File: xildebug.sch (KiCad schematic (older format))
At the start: 36 parts, among them J1 USB_B_Micro, J2 Conn_STM_SWD, J3 Conn_Ext1, J4 Conn_Ext2, J5 Conn_DUT, J6 Conn_DUT_VDD, U1 XC6206P332MR, U2 MAX14662, U3 STM32L433CCUx

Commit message: Changed the USB data pin names to match the USB connector convention
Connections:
- net USB_DM renamed USB_D+
- net USB_D+: now also J1.3 (D+); no longer J1.2 (D-)
- net USB_DP renamed USB_D-
- net USB_D-: now also J1.2 (D-); no longer J1.3 (D+)
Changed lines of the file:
@@
 Text Label 6400 5250 0    50   ~ 0
 GPIO3_A
+Text Label 4650 4250 2    50   ~ 0
+USB_D+
 Text Label 4650 4350 2    50   ~ 0
-USB_DP
-Text Label 4650 4250 2    50   ~ 0
-USB_DM
+USB_D-
 Text Label 5200 3750 2    50   ~ 0
 STM_SWDIO
@@
 $EndComp
 Text Label 2150 1650 0    50   ~ 0
-USB_DP
+USB_D+
 Text Label 2150 1750 0    50   ~ 0
-USB_DM
+USB_D-
 NoConn ~ 2100 1850
 Wire Wire Line

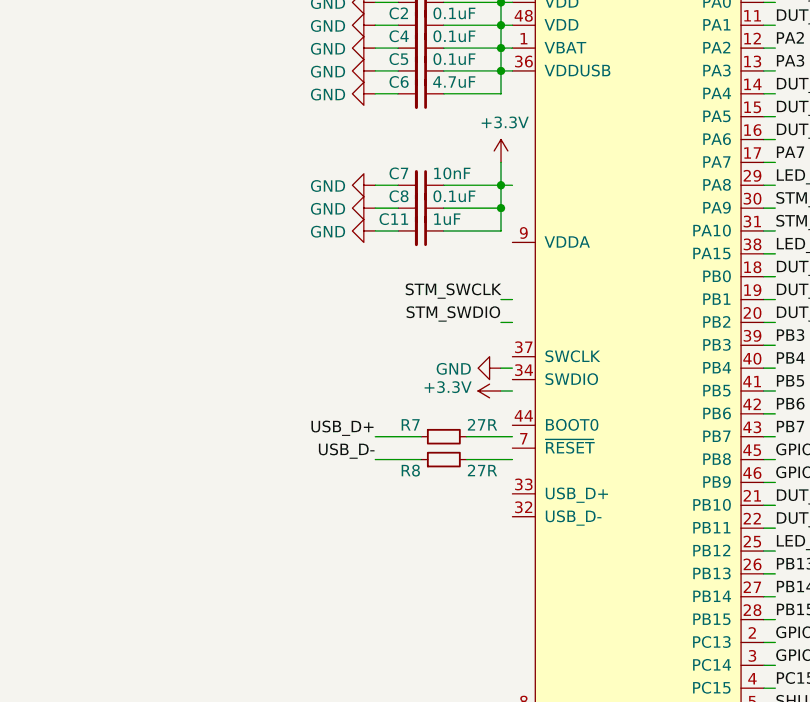
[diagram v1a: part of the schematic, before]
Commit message: Add ferrite bead on the VDDA of the STM
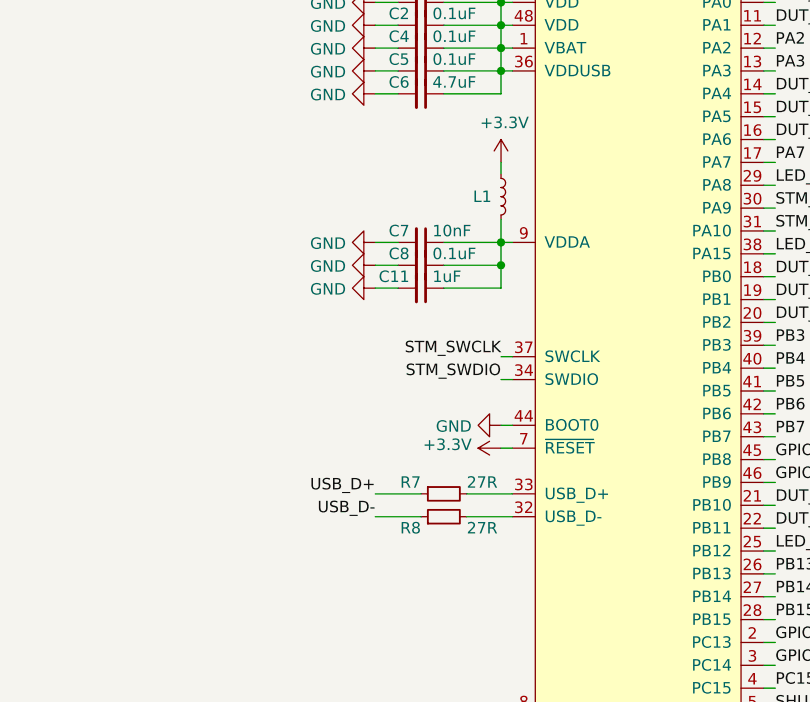
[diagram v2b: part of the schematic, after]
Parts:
- added L1: FB, symbol Device:L_Small
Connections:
- net +3V3: now also U3.7 (~RESET~), L1.2; no longer C11.1, C7.1, C8.1
- net GND: now also U3.44 (BOOT0)
- net STM_SWCLK: now also U3.37 (SWCLK)
- net STM_SWDIO: now also U3.34 (SWDIO)
- net at U3.32 (USB_D-): now also R8.2
- net at U3.33 (USB_D+): now also R7.2
- net at U3.9 (VDDA): now also C11.1, C7.1, C8.1, L1.1
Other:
- moved on the sheet: C11, C7, C8, R7, R8
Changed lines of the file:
@@
 $EndComp
 Wire Wire Line
-	5250 3750 5200 3750
-Wire Wire Line
-	5250 3650 5200 3650
+	5250 4000 5200 4000
+Wire Wire Line
+	5250 3900 5200 3900
 $Comp
 L Connector_Generic:Conn_01x06 J5
@@
 Text Label 6400 5250 0    50   ~ 0
 GPIO3_A
-Text Label 4650 4250 2    50   ~ 0
+Text Label 4650 4500 2    50   ~ 0
 USB_D+
-Text Label 4650 4350 2    50   ~ 0
+Text Label 4650 4600 2    50   ~ 0
 USB_D-
-Text Label 5200 3750 2    50   ~ 0
+Text Label 5200 4000 2    50   ~ 0
 STM_SWDIO
-Text Label 5200 3650 2    50   ~ 0
+Text Label 5200 3900 2    50   ~ 0
 STM_SWCLK
 $Comp
@@
 L Device:R_Small R8
 U 1 1 5B52EFB9
-P 4950 4350
-F 0 "R8" V 4900 4450 50  0000 L CNN
-F 1 "27R" V 4900 4250 50  0000 R CNN
-F 2 "Resistor_SMD:R_0603_1608Metric" H 4950 4350 50  0001 C CNN
-F 3 "~" H 4950 4350 50  0001 C CNN
-	1    4950 4350
+P 4950 4600
+F 0 "R8" V 4900 4700 50  0000 L CNN
+F 1 "27R" V 4900 4500 50  0000 R CNN
+F 2 "Resistor_SMD:R_0603_1608Metric" H 4950 4600 50  0001 C CNN
+F 3 "~" H 4950 4600 50  0001 C CNN
+	1    4950 4600
 	0    -1   -1   0
 $EndComp
@@
 L Device:R_Small R7
 U 1 1 5B52F1AA
-P 4950 4250
-F 0 "R7" V 4900 4350 50  0000 L CNN
-F 1 "27R" V 4900 4150 50  0000 R CNN
-F 2 "Resistor_SMD:R_0603_1608Metric" H 4950 4250 50  0001 C CNN
-F 3 "~" H 4950 4250 50  0001 C CNN
-	1    4950 4250
+P 4950 4500
+F 0 "R7" V 4900 4600 50  0000 L CNN
+F 1 "27R" V 4900 4400 50  0000 R CNN
+F 2 "Resistor_SMD:R_0603_1608Metric" H 4950 4500 50  0001 C CNN
+F 3 "~" H 4950 4500 50  0001 C CNN
+	1    4950 4500
 	0    -1   1    0
 $EndComp
 Wire Wire Line
-	5050 4350 5250 4350
-Wire Wire Line
-	5050 4250 5250 4250
-Wire Wire Line
-	4650 4350 4850 4350
-Wire Wire Line
-	4650 4250 4850 4250
+	5050 4600 5250 4600
+Wire Wire Line
+	5050 4500 5250 4500
+Wire Wire Line
+	4650 4600 4850 4600
+Wire Wire Line
+	4650 4500 4850 4500
 Wire Wire Line
 	9950 2900 10000 2900
@@
 Connection ~ 5200 5550
 Wire Wire Line
-	5250 3950 5200 3950
-Wire Wire Line
-	5250 4050 5200 4050
+	5250 4200 5200 4200
+Wire Wire Line
+	5250 4300 5200 4300
 Wire Wire Line
 	5250 2350 5200 2350
@@
 Connection ~ 5200 2550
 Wire Wire Line
-	5250 3150 5200 3150
-Wire Wire Line
-	5200 3150 5200 3050
+	5250 3400 5200 3400
 Connection ~ 5200 2650
 Wire Wire Line
 	5200 2750 5200 2650
-Connection ~ 5200 3150
-Wire Wire Line
-	5200 3150 5200 3250
-Wire Wire Line
-	5200 3250 5200 3350
-Connection ~ 5200 3250
+Connection ~ 5200 3400
+Wire Wire Line
+	5200 3400 5200 3500
+Wire Wire Line
+	5200 3500 5200 3600
+Connection ~ 5200 3500
 $Comp
 L power:+3.3V #PWR06
@@
 	4950 2450 5200 2450
 Wire Wire Line
-	4950 3150 5200 3150
-Wire Wire Line
-	4950 3250 5200 3250
-Wire Wire Line
-	4950 3350 5200 3350
+	4950 3400 5200 3400
+Wire Wire Line
+	4950 3500 5200 3500
+Wire Wire Line
+	4950 3600 5200 3600
 $Comp
 L power:GND #PWR08
@@
 L Device:C_Small C8
 U 1 1 5AF46D36
-P 4850 3250
-F 0 "C8" V 4800 3200 50  0000 R CNN
-F 1 "0.1uF" V 4800 3300 50  0000 L CNN
-F 2 "Capacitor_SMD:C_0603_1608Metric" H 4850 3250 50  0001 C CNN
-F 3 "~" H 4850 3250 50  0001 C CNN
-	1    4850 3250
+P 4850 3500
+F 0 "C8" V 4800 3450 50  0000 R CNN
+F 1 "0.1uF" V 4800 3550 50  0000 L CNN
+F 2 "Capacitor_SMD:C_0603_1608Metric" H 4850 3500 50  0001 C CNN
+F 3 "~" H 4850 3500 50  0001 C CNN
+	1    4850 3500
 	0    1    1    0
 $EndComp
@@
 L Device:C_Small C7
 U 1 1 5AF46DB8
-P 4850 3150
-F 0 "C7" V 4800 3100 50  0000 R CNN
-F 1 "10nF" V 4800 3200 50  0000 L CNN
-F 2 "Capacitor_SMD:C_0603_1608Metric" H 4850 3150 50  0001 C CNN
-F 3 "~" H 4850 3150 50  0001 C CNN
-	1    4850 3150
+P 4850 3400
+F 0 "C7" V 4800 3350 50  0000 R CNN
+F 1 "10nF" V 4800 3450 50  0000 L CNN
+F 2 "Capacitor_SMD:C_0603_1608Metric" H 4850 3400 50  0001 C CNN
+F 3 "~" H 4850 3400 50  0001 C CNN
+	1    4850 3400
 	0    1    1    0
 $EndComp
@@
 L Device:C_Small C11
 U 1 1 5AF46E6F
-P 4850 3350
-F 0 "C11" V 4800 3300 50  0000 R CNN
-F 1 "1uF" V 4800 3400 50  0000 L CNN
-F 2 "Capacitor_SMD:C_0603_1608Metric" H 4850 3350 50  0001 C CNN
-F 3 "~" H 4850 3350 50  0001 C CNN
-	1    4850 3350
-	0    1    1    0
-$EndComp
-Wire Wire Line
-	4750 3150 4650 3150
-Wire Wire Line
-	4750 3250 4650 3250
-Wire Wire Line
-	4750 3350 4650 3350
+P 4850 3600
+F 0 "C11" V 4800 3550 50  0000 R CNN
+F 1 "1uF" V 4800 3650 50  0000 L CNN
+F 2 "Capacitor_SMD:C_0603_1608Metric" H 4850 3600 50  0001 C CNN
+F 3 "~" H 4850 3600 50  0001 C CNN
+	1    4850 3600
+	0    1    1    0
+$EndComp
+Wire Wire Line
+	4750 3400 4650 3400
+Wire Wire Line
+	4750 3500 4650 3500
+Wire Wire Line
+	4750 3600 4650 3600
 $Comp
 L power:GND #PWR020
 U 1 1 5AF5E9A3
-P 4650 3150
-F 0 "#PWR020" H 4650 2900 50  0001 C CNN
-F 1 "GND" V 4655 3022 50  0000 R CNN
-F 2 "" H 4650 3150 50  0001 C CNN
-F 3 "" H 4650 3150 50  0001 C CNN
-	1    4650 3150
+P 4650 3400
+F 0 "#PWR020" H 4650 3150 50  0001 C CNN
+F 1 "GND" V 4655 3272 50  0000 R CNN
+F 2 "" H 4650 3400 50  0001 C CNN
+F 3 "" H 4650 3400 50  0001 C CNN
+	1    4650 3400
 	0    1    1    0
 $EndComp
@@
 L power:GND #PWR021
 U 1 1 5AF5EA1C
-P 4650 3250
-F 0 "#PWR021" H 4650 3000 50  0001 C CNN
-F 1 "GND" V 4655 3122 50  0000 R CNN
-F 2 "" H 4650 3250 50  0001 C CNN
-F 3 "" H 4650 3250 50  0001 C CNN
-	1    4650 3250
+P 4650 3500
+F 0 "#PWR021" H 4650 3250 50  0001 C CNN
+F 1 "GND" V 4655 3372 50  0000 R CNN
+F 2 "" H 4650 3500 50  0001 C CNN
+F 3 "" H 4650 3500 50  0001 C CNN
+	1    4650 3500
 	0    1    1    0
 $EndComp
@@
 L power:GND #PWR023
 U 1 1 5AF5EA9A
-P 4650 3350
-F 0 "#PWR023" H 4650 3100 50  0001 C CNN
-F 1 "GND" V 4655 3222 50  0000 R CNN
-F 2 "" H 4650 3350 50  0001 C CNN
-F 3 "" H 4650 3350 50  0001 C CNN
-	1    4650 3350
+P 4650 3600
+F 0 "#PWR023" H 4650 3350 50  0001 C CNN
+F 1 "GND" V 4655 3472 50  0000 R CNN
+F 2 "" H 4650 3600 50  0001 C CNN
+F 3 "" H 4650 3600 50  0001 C CNN
+	1    4650 3600
 	0    1    1    0
 $EndComp
@@
 L power:+3.3V #PWR028
 U 1 1 5AFC13F1
-P 5200 4050
-F 0 "#PWR028" H 5200 3900 50  0001 C CNN
-F 1 "+3.3V" V 5215 4178 50  0000 L CNN
-F 2 "" H 5200 4050 50  0001 C CNN
-F 3 "" H 5200 4050 50  0001 C CNN
-	1    5200 4050
+P 5200 4300
+F 0 "#PWR028" H 5200 4150 50  0001 C CNN
+F 1 "+3.3V" V 5215 4428 50  0000 L CNN
+F 2 "" H 5200 4300 50  0001 C CNN
+F 3 "" H 5200 4300 50  0001 C CNN
+	1    5200 4300
 	0    -1   -1   0
 $EndComp
@@
 L power:GND #PWR0101
 U 1 1 5BB12C8D
-P 5200 3950
-F 0 "#PWR0101" H 5200 3700 50  0001 C CNN
-F 1 "GND" V 5205 3822 50  0000 R CNN
-F 2 "" H 5200 3950 50  0001 C CNN
-F 3 "" H 5200 3950 50  0001 C CNN
-	1    5200 3950
+P 5200 4200
+F 0 "#PWR0101" H 5200 3950 50  0001 C CNN
+F 1 "GND" V 5205 4072 50  0000 R CNN
+F 2 "" H 5200 4200 50  0001 C CNN
+F 3 "" H 5200 4200 50  0001 C CNN
+	1    5200 4200
 	0    1    1    0
 $EndComp
 Text Notes 9550 3800 2    50   ~ 0
 I2C: 0x98
+$Comp
+L Device:L_Small L1
+U 1 1 5BBB5951
+P 5200 3200
+F 0 "L1" H 5159 3200 50  0000 R CNN
+F 1 "FB" H 5159 3245 50  0001 R CNN
+F 2 "" H 5200 3200 50  0001 C CNN
+F 3 "~" H 5200 3200 50  0001 C CNN
+	1    5200 3200
+	1    0    0    1
+$EndComp
+Wire Wire Line
+	5200 3100 5200 3050
+Wire Wire Line
+	5200 3300 5200 3400
 $EndSCHEMATC

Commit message: Add footprint for the STM that works for QFN and QFP
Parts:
- L1: footprint (none) -> Inductor_SMD:L_0603_1608Metric
- U3: footprint Package_DFN_QFN:QFN-48-1EP_7x7mm_P0.5mm_EP5.15x5.15mm -> Package_DFN_QFN_Extra:UFQFPN-48-1EP_7x7mm_P0.5mm_EP5.15x5.15mm
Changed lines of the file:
@@
 F 0 "U3" H 6250 5700 50  0000 R CNN
 F 1 "STM32L433CCUx" H 5800 2200 50  0000 C CNN
-F 2 "Package_DFN_QFN:QFN-48-1EP_7x7mm_P0.5mm_EP5.15x5.15mm" H 5800 2100 50  0001 C CNN
+F 2 "Package_DFN_QFN_Extra:UFQFPN-48-1EP_7x7mm_P0.5mm_EP5.15x5.15mm" H 5800 2100 50  0001 C CNN
 F 3 "https://www.mouser.se/datasheet/2/389/stm32l433cc-956250.pdf" H 5800 2100 50  0001 C CNN
 	1    5800 3950
@@
 F 0 "L1" H 5159 3200 50  0000 R CNN
 F 1 "FB" H 5159 3245 50  0001 R CNN
-F 2 "" H 5200 3200 50  0001 C CNN
+F 2 "Inductor_SMD:L_0603_1608Metric" H 5200 3200 50  0001 C CNN
 F 3 "~" H 5200 3200 50  0001 C CNN
 	1    5200 3200

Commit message: Route the PCB
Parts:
- J4: footprint Connector_PinHeader_2.54mm:PinHeader_1x11_P2.54mm_Vertical -> Connector_PinHeader_2.54mm:PinHeader_1x12_P2.54mm_Vertical; symbol Connector_Generic:Conn_01x11 -> Connector_Generic:Conn_01x12
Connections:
- net DUT_SWCLK_A: now also U2.5 (A4); no longer U2.2 (A1)
- net DUT_SWCLK_B: now also U2.18 (B4); no longer U2.21 (B1)
- net DUT_SWDIO_A: now also U2.4 (A3); no longer U2.3 (A2)
- net DUT_SWDIO_B: now also U2.19 (B3); no longer U2.20 (B2)
- net DUT_SWD_LED: now also U3.14 (PA4); no longer U3.18 (PB0)
- net DUT_UART_RX_A: now also U2.2 (A1); no longer U2.5 (A4)
- net DUT_UART_RX_LED: now also U3.6 (PH1); no longer U3.15 (PA5)
- net DUT_UART_TX_A: now also U2.3 (A2); no longer U2.4 (A3)
- net DUT_UART_TX_LED: now also U3.5 (PH0); no longer U3.14 (PA4)
- net DUT_VDD_EN: now also U3.18 (PB0); no longer U3.16 (PA6)
- net DUT_VDD_OUT: now also J3.11 (Pin_11)
- net GPIO0_A: now also U2.9 (A8); no longer U2.6 (A5)
- net GPIO0_B: now also J4.9 (Pin_9), U2.14 (B8); no longer J3.4 (Pin_4), U2.17 (B5)
- net GPIO1_A: now also U2.8 (A7); no longer U2.7 (A6)
- net GPIO1_B: now also J4.10 (Pin_10), U2.15 (B7); no longer J3.5 (Pin_5), U2.16 (B6)
- net GPIO2_A: now also U2.7 (A6); no longer U2.8 (A7)
- net GPIO2_B: now also J4.11 (Pin_11), U2.16 (B6); no longer J3.6 (Pin_6), U2.15 (B7)
- net GPIO3_A: now also U2.6 (A5); no longer U2.9 (A8)
- net GPIO3_B: now also J4.12 (Pin_12), U2.17 (B5); no longer J3.7 (Pin_7), U2.14 (B8)
- net PA2: now also J3.9 (Pin_9); no longer J4.4 (Pin_4)
- net PA3: now also J3.8 (Pin_8); no longer J4.5 (Pin_5)
- net PA7: now also J3.7 (Pin_7); no longer J4.6 (Pin_6)
- net PB13: now also J3.6 (Pin_6); no longer J3.8 (Pin_8)
- net PB14: now also J3.5 (Pin_5); no longer J3.9 (Pin_9)
- net PB15: now also J3.4 (Pin_4); no longer J3.10 (Pin_10)
- net PB3: now also J4.4 (Pin_4); no longer J4.7 (Pin_7)
- net PB4: now also J4.5 (Pin_5); no longer J4.8 (Pin_8)
- net PB5: now also J4.6 (Pin_6); no longer J4.9 (Pin_9)
- net PB6: now also J4.7 (Pin_7); no longer J4.10 (Pin_10)
- net PB7: now also J4.8 (Pin_8); no longer J4.11 (Pin_11)
- net PC15: now also J3.10 (Pin_10); no longer J3.11 (Pin_11)
- net SHUNT1_EN: now also U3.15 (PA5); no longer U3.5 (PH0)
- net SHUNT2_EN: now also U3.16 (PA6); no longer U3.6 (PH1)
- net at D6.1 (K): now also U2.21 (B1); no longer U2.18 (B4)
- net at D5.2 (A): now also U2.20 (B2); no longer U2.19 (B3)
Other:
- moved on the sheet: D5, D6
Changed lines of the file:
@@
 	9950 2800 10000 2800
-Wire Wire Line
-	9950 3400 10000 3400
-Wire Wire Line
-	9950 3500 10000 3500
 Wire Wire Line
 	8950 2700 8900 2700
@@
 Text Label 3000 7400 0    50   ~ 0
 DUT_UART_TX_B
-Text Label 10000 3400 0    50   ~ 0
+Text Label 10000 3700 0    50   ~ 0
 DUT_SWCLK_B
-Text Label 10000 3500 0    50   ~ 0
+Text Label 10000 3600 0    50   ~ 0
 DUT_SWDIO_B
-Text Label 10300 3600 0    50   ~ 0
+Text Label 10300 3500 0    50   ~ 0
 DUT_UART_TX_B
-Text Label 10300 3700 0    50   ~ 0
+Text Label 10300 3400 0    50   ~ 0
 DUT_UART_RX_B
 Text Label 8900 2700 2    50   ~ 0
@@
 Text Label 6400 3750 0    50   ~ 0
 DUT_SWDIO_A
-Text Label 10000 2500 0    50   ~ 0
+Text Label 10000 2800 0    50   ~ 0
 DUT_SWCLK_A
-Text Label 10000 2600 0    50   ~ 0
+Text Label 10000 2700 0    50   ~ 0
 DUT_SWDIO_A
 Text Label 6400 4550 0    50   ~ 0
@@
 Text Label 6400 4650 0    50   ~ 0
 DUT_UART_RX_A
-Text Label 10000 2700 0    50   ~ 0
+Text Label 10000 2600 0    50   ~ 0
 DUT_UART_TX_A
-Text Label 10000 2800 0    50   ~ 0
+Text Label 10000 2500 0    50   ~ 0
 DUT_UART_RX_A
-Text Label 6400 2950 0    50   ~ 0
+Text Label 6400 3550 0    50   ~ 0
 DUT_VDD_EN
 Text Label 6400 2350 0    50   ~ 0
@@
 Text Label 6400 3350 0    50   ~ 0
 STM_SDA
+Text Label 6400 2850 0    50   ~ 0
+SHUNT1_EN
+Text Label 6400 2950 0    50   ~ 0
+SHUNT2_EN
 Text Label 6400 5450 0    50   ~ 0
-SHUNT1_EN
+DUT_UART_TX_LED
 Text Label 6400 5550 0    50   ~ 0
-SHUNT2_EN
-Text Label 6400 2750 0    50   ~ 0
-DUT_UART_TX_LED
-Text Label 6400 2850 0    50   ~ 0
 DUT_UART_RX_LED
-Text Label 1000 7100 0    50   ~ 0
+Text Label 2000 7600 0    50   ~ 0
 GPIO3_B
-Text Label 1000 6800 0    50   ~ 0
+Text Label 2000 7300 0    50   ~ 0
 GPIO0_B
-Text Label 1000 7000 0    50   ~ 0
+Text Label 2000 7500 0    50   ~ 0
 GPIO2_B
-Text Label 1000 6900 0    50   ~ 0
+Text Label 2000 7400 0    50   ~ 0
 GPIO1_B
 Text Label 6350 850  0    50   ~ 0
@@
 	2000 7200 1950 7200
 $Comp
-L Connector_Generic:Conn_01x11 J4
+L Connector_Generic:Conn_01x12 J4
 U 1 1 5B12D19C
 P 1750 7000
 F 0 "J4" H 1750 7600 50  0000 C CNN
 F 1 "Conn_Ext2" V 1850 7000 50  0000 C CNN
-F 2 "Connector_PinHeader_2.54mm:PinHeader_1x11_P2.54mm_Vertical" H 1750 7000 50  0001 C CNN
+F 2 "Connector_PinHeader_2.54mm:PinHeader_1x12_P2.54mm_Vertical" H 1750 7000 50  0001 C CNN
 F 3 "~" H 1750 7000 50  0001 C CNN
 	1    1750 7000
@@
 L Device:D_Small D5
 U 1 1 5B47A1D1
-P 10150 3600
-F 0 "D5" H 10200 3650 50  0000 L CNN
-F 1 "D_TX" H 10150 3714 50  0001 C CNN
-F 2 "Diode_SMD:D_SOD-323_HandSoldering" V 10150 3600 50  0001 C CNN
-F 3 "~" V 10150 3600 50  0001 C CNN
-	1    10150 3600
+P 10150 3500
+F 0 "D5" H 10200 3550 50  0000 L CNN
+F 1 "D_TX" H 10150 3614 50  0001 C CNN
+F 2 "Diode_SMD:D_SOD-323_HandSoldering" V 10150 3500 50  0001 C CNN
+F 3 "~" V 10150 3500 50  0001 C CNN
+	1    10150 3500
 	-1   0    0    -1
 $EndComp
@@
 L Device:D_Small D6
 U 1 1 5B47A350
-P 10150 3700
-F 0 "D6" H 10100 3750 50  0000 R CNN
-F 1 "D_RX" H 10150 3814 50  0001 C CNN
-F 2 "Diode_SMD:D_SOD-323_HandSoldering" V 10150 3700 50  0001 C CNN
-F 3 "~" V 10150 3700 50  0001 C CNN
-	1    10150 3700
-	1    0    0    -1
-$EndComp
-Wire Wire Line
-	9950 3600 10050 3600
-Wire Wire Line
-	9950 3700 10050 3700
-Wire Wire Line
-	10250 3600 10300 3600
-Wire Wire Line
-	10300 3700 10250 3700
+P 10150 3400
+F 0 "D6" H 10100 3450 50  0000 R CNN
+F 1 "D_RX" H 10150 3514 50  0001 C CNN
+F 2 "Diode_SMD:D_SOD-323_HandSoldering" V 10150 3400 50  0001 C CNN
+F 3 "~" V 10150 3400 50  0001 C CNN
+	1    10150 3400
+	1    0    0    -1
+$EndComp
+Wire Wire Line
+	9950 3500 10050 3500
+Wire Wire Line
+	9950 3400 10050 3400
+Wire Wire Line
+	10250 3500 10300 3500
+Wire Wire Line
+	10300 3400 10250 3400
 $Comp
 L Device:R_Small R8
@@
 Wire Wire Line
 	9950 4100 10000 4100
+Text Label 10000 3200 0    50   ~ 0
+GPIO0_A
+Text Label 10000 3100 0    50   ~ 0
+GPIO1_A
+Text Label 10000 3000 0    50   ~ 0
+GPIO2_A
 Text Label 10000 2900 0    50   ~ 0
-GPIO0_A
-Text Label 10000 3000 0    50   ~ 0
-GPIO1_A
-Text Label 10000 3100 0    50   ~ 0
-GPIO2_A
-Text Label 10000 3200 0    50   ~ 0
 GPIO3_A
+Text Label 10000 3800 0    50   ~ 0
+GPIO3_B
 Text Label 10000 4100 0    50   ~ 0
-GPIO3_B
-Text Label 10000 3800 0    50   ~ 0
 GPIO0_B
+Text Label 10000 3900 0    50   ~ 0
+GPIO2_B
 Text Label 10000 4000 0    50   ~ 0
-GPIO2_B
-Text Label 10000 3900 0    50   ~ 0
 GPIO1_B
 $Comp
@@
 	0    -1   -1   0
 $EndComp
-Text Label 6400 3550 0    50   ~ 0
+Text Label 6400 2750 0    50   ~ 0
 DUT_SWD_LED
 Text Label 6350 700  0    50   ~ 0
@@
 Text Label 6400 5350 0    50   ~ 0
 PC15
+Text Label 1000 7300 0    50   ~ 0
+PA2
+Text Label 1000 7200 0    50   ~ 0
+PA3
+Text Label 1000 7100 0    50   ~ 0
+PA7
 Text Label 2000 6800 0    50   ~ 0
-PA2
+PB3
 Text Label 2000 6900 0    50   ~ 0
-PA3
+PB4
 Text Label 2000 7000 0    50   ~ 0
-PA7
+PB5
 Text Label 2000 7100 0    50   ~ 0
-PB3
+PB6
 Text Label 2000 7200 0    50   ~ 0
-PB4
-Text Label 2000 7300 0    50   ~ 0
-PB5
-Text Label 2000 7400 0    50   ~ 0
-PB6
-Text Label 2000 7500 0    50   ~ 0
 PB7
-Text Label 1000 7200 0    50   ~ 0
+Text Label 1000 7000 0    50   ~ 0
 PB13
-Text Label 1000 7300 0    50   ~ 0
+Text Label 1000 6900 0    50   ~ 0
 PB14
+Text Label 1000 6800 0    50   ~ 0
+PB15
 Text Label 1000 7400 0    50   ~ 0
-PB15
-Text Label 1000 7500 0    50   ~ 0
 PC15
 $Sheet
@@
 Wire Wire Line
 	5200 3300 5200 3400
+Wire Wire Line
+	1950 7600 2000 7600
+Text Label 1000 7500 0    50   ~ 0
+DUT_VDD_OUT
+Wire Wire Line
+	10000 3600 9950 3600
+Wire Wire Line
+	10000 3700 9950 3700
 $EndSCHEMATC
